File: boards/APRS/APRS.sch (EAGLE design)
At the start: 20 parts

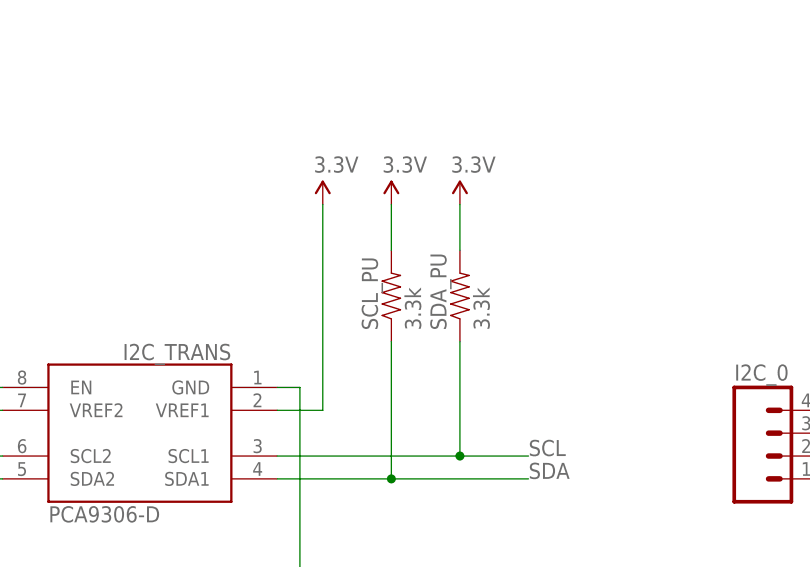
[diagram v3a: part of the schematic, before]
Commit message: Fixed misnamed I2C pull-ups
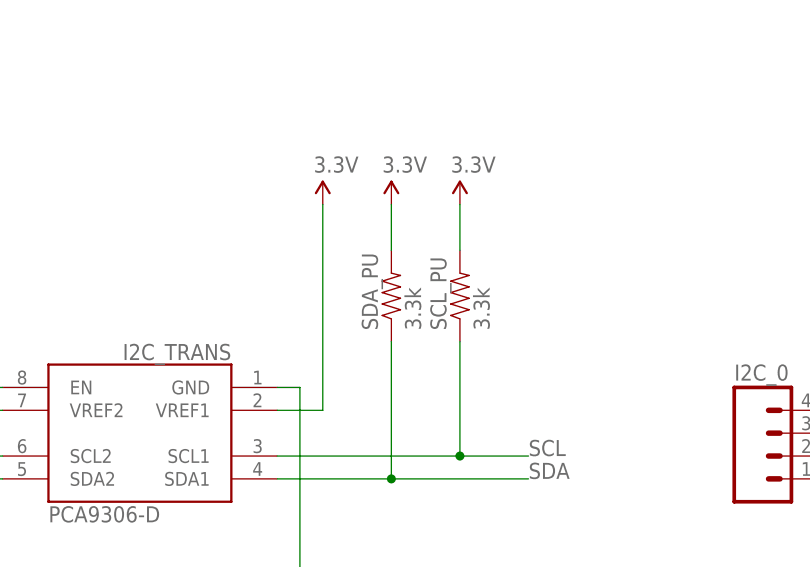
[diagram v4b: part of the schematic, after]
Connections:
- net SCL: now also SCL_PU.1; no longer SDA_PU.1
- net SDA: now also SDA_PU.1; no longer SCL_PU.1
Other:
- moved on the sheet: SCL_PU, SDA_PU
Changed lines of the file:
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@@
 <part name="P+5" library="SparkFun-Aesthetics" deviceset="3.3V" device=""/>
 <part name="P+6" library="SparkFun-Aesthetics" deviceset="3.3V" device=""/>
+<part name="SDA_PU" library="SparkFun-Passives" deviceset="RESISTOR" device="0805-RES" value="3.3k"/>
 <part name="SCL_PU" library="SparkFun-Passives" deviceset="RESISTOR" device="0805-RES" value="3.3k"/>
-<part name="SDA_PU" library="SparkFun-Passives" deviceset="RESISTOR" device="0805-RES" value="3.3k"/>
 <part name="U$9" library="SparkFun-Aesthetics" deviceset="5V" device=""/>
 <part name="I2C_0" library="SparkFun-Connectors" deviceset="M04" device="PTH"/>
@@
 <instance part="P+5" gate="G$1" x="243.84" y="58.42"/>
 <instance part="P+6" gate="G$1" x="251.46" y="58.42"/>
-<instance part="SCL_PU" gate="G$1" x="243.84" y="48.26" rot="R90"/>
-<instance part="SDA_PU" gate="G$1" x="251.46" y="48.26" rot="R90"/>
+<instance part="SDA_PU" gate="G$1" x="243.84" y="48.26" rot="R90"/>
+<instance part="SCL_PU" gate="G$1" x="251.46" y="48.26" rot="R90"/>
 <instance part="U$9" gate="G$1" x="198.12" y="58.42"/>
 <instance part="I2C_0" gate="G$1" x="287.02" y="30.48"/>
@@
 <segment>
 <pinref part="P+5" gate="G$1" pin="3.3V"/>
+<pinref part="SDA_PU" gate="G$1" pin="2"/>
+<wire x1="243.84" y1="58.42" x2="243.84" y2="53.34" width="0.1524" layer="91"/>
+</segment>
+<segment>
+<pinref part="P+6" gate="G$1" pin="3.3V"/>
 <pinref part="SCL_PU" gate="G$1" pin="2"/>
-<wire x1="243.84" y1="58.42" x2="243.84" y2="53.34" width="0.1524" layer="91"/>
-</segment>
-<segment>
-<pinref part="P+6" gate="G$1" pin="3.3V"/>
-<pinref part="SDA_PU" gate="G$1" pin="2"/>
 <wire x1="251.46" y1="58.42" x2="251.46" y2="53.34" width="0.1524" layer="91"/>
 </segment>
@@
 <wire x1="231.14" y1="30.48" x2="251.46" y2="30.48" width="0.1524" layer="91"/>
 <label x="259.08" y="30.48" size="1.778" layer="95"/>
-<pinref part="SDA_PU" gate="G$1" pin="1"/>
+<pinref part="SCL_PU" gate="G$1" pin="1"/>
 <wire x1="251.46" y1="30.48" x2="259.08" y2="30.48" width="0.1524" layer="91"/>
 <wire x1="251.46" y1="43.18" x2="251.46" y2="30.48" width="0.1524" layer="91"/>
@@
 <wire x1="231.14" y1="27.94" x2="243.84" y2="27.94" width="0.1524" layer="91"/>
 <label x="259.08" y="27.94" size="1.778" layer="95"/>
-<pinref part="SCL_PU" gate="G$1" pin="1"/>
+<pinref part="SDA_PU" gate="G$1" pin="1"/>
 <wire x1="243.84" y1="27.94" x2="259.08" y2="27.94" width="0.1524" layer="91"/>
 <wire x1="243.84" y1="43.18" x2="243.84" y2="27.94" width="0.1524" layer="91"/>

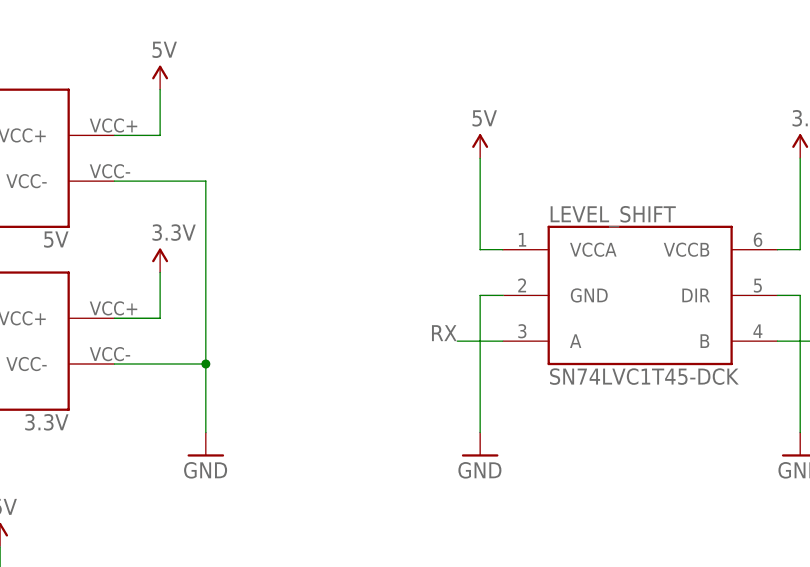
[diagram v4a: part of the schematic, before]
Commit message: APRS v4 -- Added RX_EN
I couldn't solder the Arduino board directly because the level
shifter was breaking uploading sketches, so I added an RX_EN
jumper.
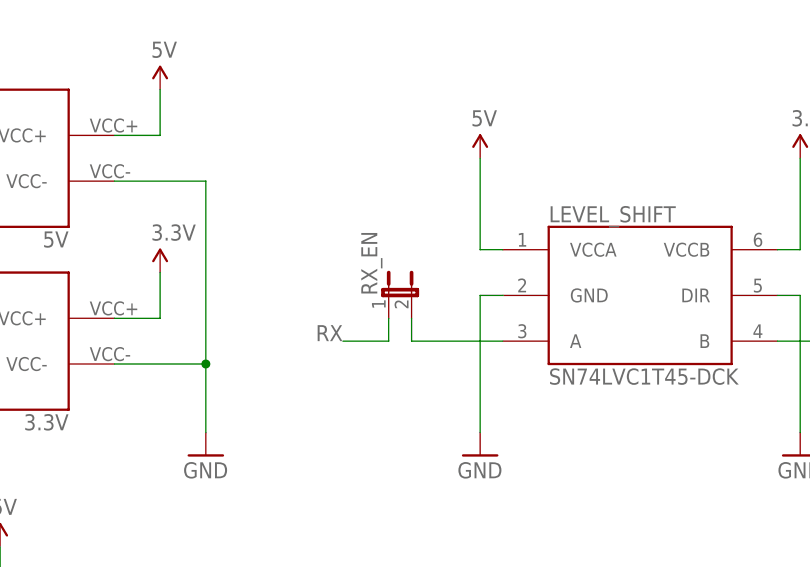
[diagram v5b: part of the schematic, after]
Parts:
- added RX_EN: (no value), SparkFun-Passives:JUMPER-2PTH
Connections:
- new net N$7: LEVEL_SHIFT.A, RX_EN.2
- net RX: now also RX_EN.1; no longer LEVEL_SHIFT.A
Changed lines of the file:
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@@
 <part name="GND14" library="SparkFun-Aesthetics" deviceset="GND" device=""/>
 <part name="U$11" library="SparkFun-Aesthetics" deviceset="5V" device=""/>
+<part name="RX_EN" library="SparkFun-Passives" deviceset="JUMPER-2" device="PTH"/>
 </parts>
 <sheets>
@@
 <instance part="GND14" gate="1" x="27.94" y="50.8"/>
 <instance part="U$11" gate="G$1" x="68.58" y="76.2"/>
+<instance part="RX_EN" gate="A" x="111.76" y="104.14"/>
 </instances>
 <busses>
@@
 </segment>
 <segment>
-<pinref part="LEVEL_SHIFT" gate="G$1" pin="A"/>
-<wire x1="124.46" y1="99.06" x2="119.38" y2="99.06" width="0.1524" layer="91"/>
-<label x="119.38" y="99.06" size="1.778" layer="95" rot="MR0"/>
+<pinref part="RX_EN" gate="A" pin="1"/>
+<wire x1="111.76" y1="101.6" x2="111.76" y2="99.06" width="0.1524" layer="91"/>
+<wire x1="111.76" y1="99.06" x2="106.68" y2="99.06" width="0.1524" layer="91"/>
+<label x="106.68" y="99.06" size="1.778" layer="95" rot="MR0"/>
 </segment>
 </net>
@@
 </segment>
 </net>
+<net name="N$7" class="0">
+<segment>
+<pinref part="LEVEL_SHIFT" gate="G$1" pin="A"/>
+<pinref part="RX_EN" gate="A" pin="2"/>
+<wire x1="124.46" y1="99.06" x2="114.3" y2="99.06" width="0.1524" layer="91"/>
+<wire x1="114.3" y1="99.06" x2="114.3" y2="101.6" width="0.1524" layer="91"/>
+</segment>
+</net>
